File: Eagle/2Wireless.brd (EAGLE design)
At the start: 62.7 x 33 mm, 19 parts, among them IC1 TCA9517A, IC3 MB85RS2MTAPNF-G-BDERE1

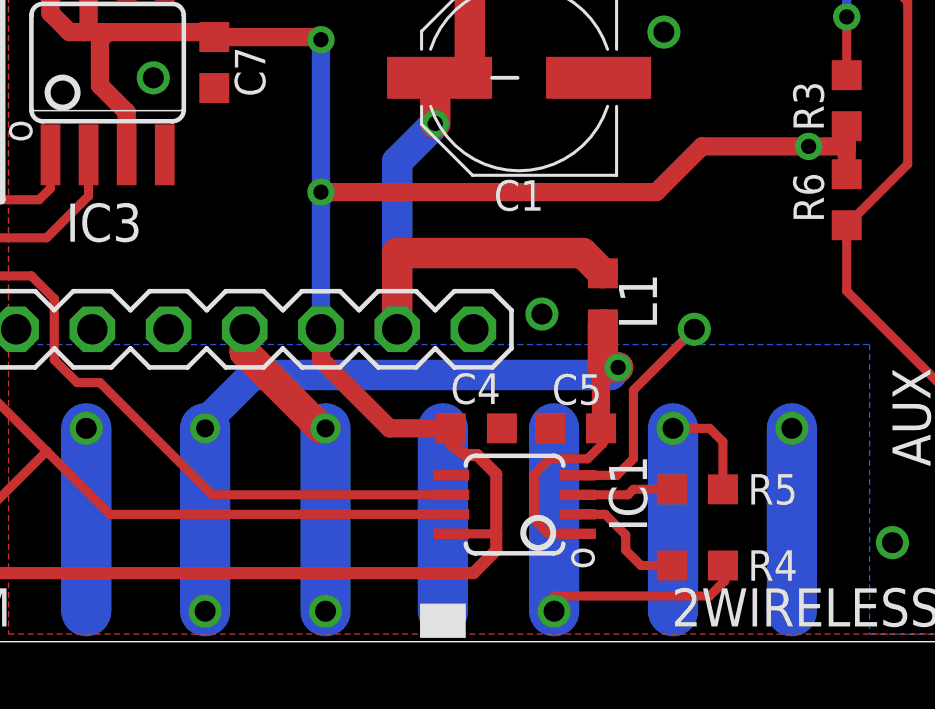
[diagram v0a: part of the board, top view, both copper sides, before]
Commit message: Change power source on TCA9517A.
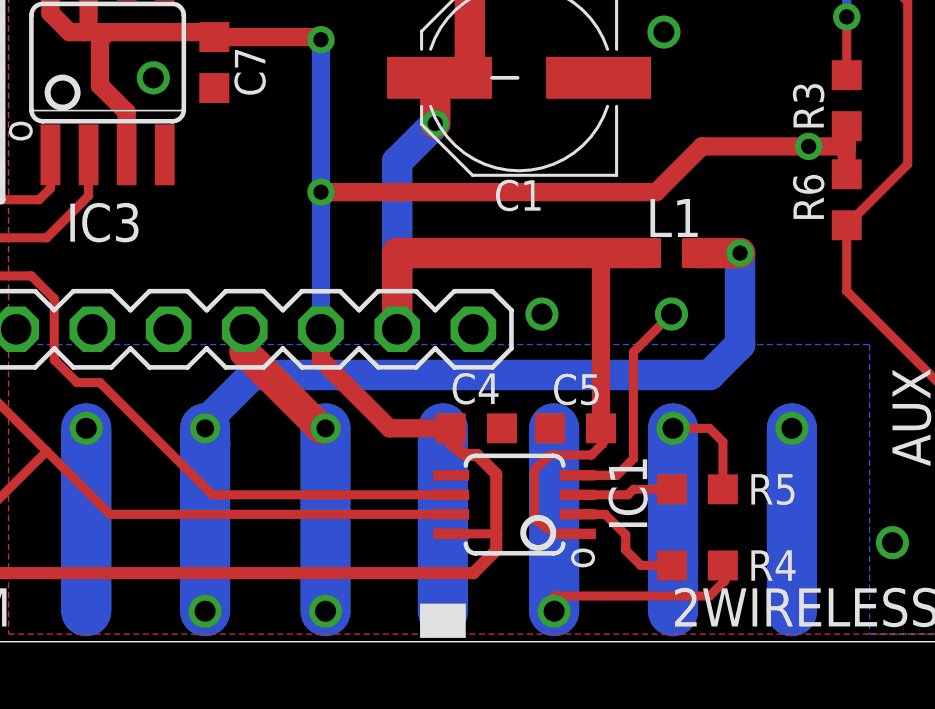
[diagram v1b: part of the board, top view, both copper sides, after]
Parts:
- moved L1 2.75 mm to (45.2, 13.0), turned to 180 degrees
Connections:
- net +5V: now also C5.1, IC1.1
- net EDAC-5V+: no longer C5.1, IC1.1
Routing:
- net +5V: track 29.4 -> 42.9 mm
- net EDAC-5V+: track 31.7 -> 30.7 mm
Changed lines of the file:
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@@
 <attribute name="VALUE" x="36.449" y="24.332" size="1.016" layer="27" font="vector" ratio="12" rot="R180"/>
 </element>
-<element name="L1" library="studio_h" package="0603" value="" x="42.926" y="11.43" smashed="yes" rot="R90">
-<attribute name="Z_MOUSER" value="710-742792609" x="41.91" y="3.048" size="1.778" layer="27" rot="R90" display="off"/>
-<attribute name="Z_SMT" value="Y" x="41.91" y="3.048" size="1.778" layer="27" rot="R90" display="off"/>
-<attribute name="MF" value="WURTH" x="41.91" y="3.048" size="1.778" layer="27" rot="R90" display="off"/>
-<attribute name="MPN" value="742792609" x="41.91" y="3.048" size="1.778" layer="27" rot="R90" display="off"/>
-<attribute name="Z_DIGIKEY" value="732-1591-1-ND" x="41.91" y="3.048" size="1.778" layer="27" rot="R90" display="off"/>
-<attribute name="NAME" x="44.7302" y="10.414" size="1.27" layer="25" font="vector" ratio="12" rot="R90"/>
-<attribute name="VALUE" x="44.906" y="10.795" size="1.27" layer="27" font="vector" ratio="12" rot="R90"/>
+<element name="L1" library="studio_h" package="0603" value="" x="45.212" y="12.954" smashed="yes" rot="R180">
+<attribute name="Z_MOUSER" value="710-742792609" x="53.594" y="11.938" size="1.778" layer="27" rot="R180" display="off"/>
+<attribute name="Z_SMT" value="Y" x="53.594" y="11.938" size="1.778" layer="27" rot="R180" display="off"/>
+<attribute name="MF" value="WURTH" x="53.594" y="11.938" size="1.778" layer="27" rot="R180" display="off"/>
+<attribute name="MPN" value="742792609" x="53.594" y="11.938" size="1.778" layer="27" rot="R180" display="off"/>
+<attribute name="Z_DIGIKEY" value="732-1591-1-ND" x="53.594" y="11.938" size="1.778" layer="27" rot="R180" display="off"/>
+<attribute name="NAME" x="46.228" y="14.7582" size="1.27" layer="25" font="vector" ratio="12" rot="R180"/>
+<attribute name="VALUE" x="45.847" y="14.934" size="1.27" layer="27" font="vector" ratio="12" rot="R180"/>
 </element>
 <element name="D1" library="studio_h" package="SMA" value="DMRA4003" x="40.894" y="24.13" smashed="yes" rot="R180">
@@
 <wire x1="33.6804" y1="7.112" x2="33.782" y2="7.112" width="1.016" layer="16"/>
 <via x="40.894" y="10.922" extent="1-16" drill="0.7"/>
-<via x="45.974" y="10.414" extent="1-16" drill="0.7"/>
+<via x="45.212" y="10.922" extent="1-16" drill="0.7"/>
 <wire x1="42.0926" y1="5.546" x2="43.392" y2="5.546" width="0.3048" layer="1"/>
 <wire x1="43.392" y1="5.546" x2="43.942" y2="6.096" width="0.3048" layer="1"/>
-<wire x1="43.942" y1="6.096" x2="43.942" y2="8.382" width="0.3048" layer="1"/>
-<wire x1="43.942" y1="8.382" x2="45.974" y2="10.414" width="0.3048" layer="1"/>
+<wire x1="43.942" y1="6.096" x2="43.942" y2="9.652" width="0.3048" layer="1"/>
+<wire x1="43.942" y1="9.652" x2="45.212" y2="10.922" width="0.3048" layer="1"/>
 </signal>
 <signal name="EDAC-12V+">
@@
 <wire x1="37.338" y1="18.652" x2="37.482" y2="18.796" width="1.016" layer="1"/>
 <wire x1="36.068" y1="10.414" x2="36.068" y2="12.954" width="1.016" layer="1"/>
-<wire x1="36.068" y1="12.954" x2="42.252" y2="12.954" width="1.016" layer="1"/>
-<wire x1="42.252" y1="12.954" x2="42.926" y2="12.28" width="1.016" layer="1"/>
+<wire x1="36.068" y1="12.954" x2="42.672" y2="12.954" width="1.016" layer="1"/>
+<contactref element="IC1" pad="1"/>
+<contactref element="C5" pad="1"/>
+<wire x1="42.672" y1="12.954" x2="44.362" y2="12.954" width="1.016" layer="1"/>
+<wire x1="42.0926" y1="3.596" x2="41.362" y2="3.596" width="0.3048" layer="1"/>
+<wire x1="41.362" y1="3.596" x2="40.64" y2="4.064" width="0.3048" layer="1"/>
+<wire x1="41.148" y1="6.223" x2="42.545" y2="6.223" width="0.3048" layer="1"/>
+<wire x1="40.64" y1="4.064" x2="40.64" y2="5.715" width="0.3048" layer="1"/>
+<wire x1="40.64" y1="5.715" x2="41.148" y2="6.223" width="0.3048" layer="1"/>
+<wire x1="42.545" y1="6.223" x2="42.926" y2="6.604" width="0.3048" layer="1"/>
+<wire x1="42.926" y1="6.604" x2="42.926" y2="7.0476" width="0.3048" layer="1"/>
+<wire x1="42.926" y1="7.0476" x2="42.8616" y2="7.112" width="0.3048" layer="1"/>
+<wire x1="42.8616" y1="7.112" x2="42.8616" y2="12.7644" width="0.6096" layer="1"/>
+<wire x1="42.8616" y1="12.7644" x2="42.672" y2="12.954" width="0.6096" layer="1"/>
 </signal>
 <signal name="EDAC-5V+">
 <contactref element="L1" pad="1"/>
-<wire x1="29.6672" y1="7.112" x2="29.6672" y2="1.016" width="1.6764" layer="16"/>
-<contactref element="IC1" pad="1"/>
-<contactref element="C5" pad="1"/>
-<wire x1="42.0926" y1="3.596" x2="41.108" y2="3.596" width="0.3048" layer="1"/>
-<wire x1="41.108" y1="3.596" x2="40.64" y2="4.064" width="0.3048" layer="1"/>
+<wire x1="29.6672" y1="7.112" x2="29.6672" y2="6.604" width="1.6764" layer="16"/>
+<wire x1="29.6672" y1="6.604" x2="29.6672" y2="1.016" width="1.6764" layer="16"/>
 <wire x1="29.6672" y1="1.016" x2="29.6672" y2="1.4732" width="0.6096" layer="16"/>
 <via x="29.6672" y="1.016" extent="1-16" drill="0.7"/>
 <via x="29.6672" y="7.112" extent="1-16" drill="0.6"/>
-<wire x1="40.64" y1="4.064" x2="40.64" y2="5.588" width="0.3048" layer="1"/>
-<wire x1="40.64" y1="5.588" x2="41.148" y2="6.096" width="0.3048" layer="1"/>
-<wire x1="41.148" y1="6.096" x2="42.418" y2="6.096" width="0.3048" layer="1"/>
-<wire x1="42.418" y1="6.096" x2="42.926" y2="6.604" width="0.3048" layer="1"/>
-<wire x1="42.926" y1="6.604" x2="42.926" y2="7.0476" width="0.3048" layer="1"/>
-<wire x1="42.926" y1="7.0476" x2="42.8616" y2="7.112" width="0.3048" layer="1"/>
-<wire x1="29.718" y1="7.112" x2="29.718" y2="7.366" width="1.016" layer="16"/>
 <wire x1="29.718" y1="7.366" x2="31.242" y2="8.89" width="1.016" layer="16"/>
-<wire x1="31.242" y1="8.89" x2="43.18" y2="8.89" width="1.016" layer="16"/>
-<wire x1="43.18" y1="8.89" x2="43.434" y2="9.144" width="1.016" layer="16"/>
-<via x="43.434" y="9.144" extent="1-16" drill="0.508"/>
-<wire x1="43.434" y1="9.144" x2="42.926" y2="9.144" width="1.016" layer="1"/>
-<wire x1="42.926" y1="9.144" x2="42.926" y2="10.58" width="1.016" layer="1"/>
-<wire x1="42.8616" y1="7.112" x2="42.8616" y2="9.0796" width="0.6096" layer="1"/>
-<wire x1="42.8616" y1="9.0796" x2="42.926" y2="9.144" width="0.6096" layer="1"/>
-<wire x1="29.6672" y1="7.112" x2="29.718" y2="7.112" width="0" layer="19" extent="16-16"/>
+<wire x1="31.242" y1="8.89" x2="46.482" y2="8.89" width="1.016" layer="16"/>
+<wire x1="46.482" y1="8.89" x2="47.498" y2="9.906" width="1.016" layer="16"/>
+<wire x1="47.498" y1="9.906" x2="47.498" y2="12.954" width="1.016" layer="16"/>
+<via x="47.498" y="12.954" extent="1-16" drill="0.508"/>
+<wire x1="47.498" y1="12.954" x2="46.062" y2="12.954" width="1.016" layer="1"/>
+<wire x1="29.718" y1="7.366" x2="29.718" y2="6.6548" width="1.016" layer="16"/>
+<wire x1="29.718" y1="6.6548" x2="29.6672" y2="6.604" width="1.016" layer="16"/>
 </signal>
 <signal name="MOSI">
